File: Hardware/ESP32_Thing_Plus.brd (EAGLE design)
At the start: 33 x 58.9 mm, 54 parts, among them Q1 2.5A/30V, Q2 MBT3904DW1T1, U1 MCP73831, U2 ESP-WROOM-32, U3 AP2112K-3.3V, U4 FT231XS

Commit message: Feedback from review
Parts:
- removed C11, C14, C16, C3: 0.1uF, SparkFun-Capacitors:0603
- removed C12, C13: 47pF, SparkFun-Capacitors:0603
- removed C15: 4.7uF, SparkFun-Capacitors:0603-CAP
- removed C2: 10uF, SparkFun-Capacitors:0805
- removed D4: BLUE, SparkFun-LED:LED-0603
- removed F1: 6V/0.75A, SparkFun-Fuses:1206
- removed JP15: (no value), SparkFun-Connectors:USB-B-MICRO-SMD_V03
- removed R10: 10k, SparkFun-Resistors:0603
- removed R13, R14: 27, SparkFun-Resistors:0603
- removed S2: BTN-0, SparkFun-Electromechanical:TACTILE_SWITCH_SMD_4.6X2.8MM
- removed SJ1, SJ2: JUMPER-PAD-2-NC_BY_TRACE, SparkFun-Passives:PAD-JUMPER-2-NC_BY_TRACE_YES_SILK
- added J4: (no value), SparkFun-Connectors:1X16_NO_SILK
- added LOGO4: FOUR_LAYER_WARNING, SparkFun-Aesthetics:FOUR_LAYER_WARNING
- added R1: 1k, SparkFun-Resistors:0603
- added U$1: (no value), buzzard_labels:3V322
- added U$10: (no value), buzzard_labels:1611
- added U$11: (no value), buzzard_labels:1710
- added U$12: (no value), buzzard_labels:A020
- added U$13: (no value), buzzard_labels:A119
- added U$14: (no value), buzzard_labels:A218
- added U$15: (no value), buzzard_labels:A317
- added U$16: (no value), buzzard_labels:A416
- added U$17: (no value), buzzard_labels:A515
- added U$18: (no value), buzzard_labels:GND21
- added U$19: (no value), buzzard_labels:MISO12
- added U$2: (no value), buzzard_labels:138
- added U$20: (no value), buzzard_labels:MOSI13
- added U$21: (no value), buzzard_labels:SCK14
- added U$22: (no value), buzzard_labels:RESET23
- added U$23: (no value), buzzard_labels:SCL1
- added U$24: (no value), buzzard_labels:SDA0
- added U$25: (no value), buzzard_labels (1):CHG3
- added U$26: (no value), buzzard_labels (1):EN1
- added U$27, U$30: (no value), buzzard_labels (1):ESP32_THING_PLUS4
- added U$28: (no value), buzzard_labels (1):VBAT2
- added U$29: (no value), buzzard_labels (1):VUSB0
- added U$3: (no value), buzzard_labels:142
- added U$31: (no value), buzzard_labels (2):3V313
- added U$32: (no value), buzzard_labels (2):#RESET17
- added U$33: (no value), buzzard_labels (2):162
- added U$34: (no value), buzzard_labels (2):171
- added U$35: (no value), buzzard_labels (2):230
- added U$36: (no value), buzzard_labels (2):1326
- added U$37: (no value), buzzard_labels (2):1420
- added U$38: (no value), buzzard_labels (2):1522
- added U$39: (no value), buzzard_labels (2):2025
- added U$4: (no value), buzzard_labels:154
- added U$40: (no value), buzzard_labels (2):2724
- added U$41: (no value), buzzard_labels (2):3221
- added U$42: (no value), buzzard_labels (2):3323
- added U$43: (no value), buzzard_labels (2):A011
- added U$44: (no value), buzzard_labels (2):A29
- added U$45: (no value), buzzard_labels (2):A38
- added U$46: (no value), buzzard_labels (2):A47
- added U$47: (no value), buzzard_labels (2):A56
- added U$48: (no value), buzzard_labels (2):A110
- added U$49: (no value), buzzard_labels (2):EN16
- added U$5: (no value), buzzard_labels:207
- added U$50: (no value), buzzard_labels (2):GND12
- added U$51: (no value), buzzard_labels (2):MISO3
- added U$52: (no value), buzzard_labels (2):MOSI4
- added U$53: (no value), buzzard_labels (2):SCK5
- added U$54: (no value), buzzard_labels (2):SCL19
- added U$55: (no value), buzzard_labels (2):SDA18
- added U$56: (no value), buzzard_labels (2):VBAT15
- added U$57: (no value), buzzard_labels (2):VUSB14
- added U$58: (no value), buzzard_labels (3):QWIIC0
- added U$59: (no value), SparkFun-Aesthetics:ORDERING_INSTRUCTIONS
- added U$6: (no value), buzzard_labels:239
- added U$60: (no value), buzzard_labels (5):RESET0
- added U$7: (no value), buzzard_labels:276
- added U$8: (no value), buzzard_labels:323
- added U$9: (no value), buzzard_labels:335
- C1: value 0.1uF -> 10uF
- C10: value 2.2uF -> 1.0uF; device SparkFun-Capacitors:0603 -> SparkFun-Capacitors:0402
- D3: value RED -> BLUE
- FD1, FD2, FD3, FD4: device SparkFun-Aesthetics:MICRO-FIDUCIAL -> SparkFun-Aesthetics:FIDUCIAL-MICRO
- J1: value (none) -> AMP FCI 10103594-0001LF; device SparkFun-Connectors:1X20_NOSILK -> SparkFun-Connectors:USB-MICROB-PTH
- J2: device SparkFun-Connectors:1X20_NOSILK -> SparkFun-Connectors:1X12_NO_SILK
- JP2: device SparkFun-Connectors:JST-2-PTH -> SparkFun-Connectors:JST-2-SMD
- LOGO1: value SFE_LOGO_NAME.1_INCH -> SFE_LOGO_FLAME.1_INCH; device SparkFun-Aesthetics:SFE_LOGO_NAME_.1 -> SparkFun-Aesthetics:SFE_LOGO_FLAME_.1
- LOGO3: value SFE_LOGO_NAME.2_INCH -> SFE_LOGO_NAME_FLAME.1_INCH; device SparkFun-Aesthetics:SFE_LOGO_NAME_.2 -> SparkFun-Aesthetics:SFE_LOGO_NAME_FLAME_.1
- R4: value 1K -> 1k
- R5: value DNP -> 100K; device SparkFun-Passives:1/6W-RES -> SparkFun-Resistors:0402
- R8: value 330 -> 100K; device SparkFun-Resistors:0603 -> SparkFun-Resistors:0402
- R9: value 10k -> 100K; device SparkFun-Resistors:0603 -> SparkFun-Resistors:0402
- S1: device SparkFun-Electromechanical:TACTILE_SWITCH_SMD_4.6X2.8MM -> SparkFun-Switches:TACTILE_SWITCH_SMD_4.6X2.8MM
- U2: value ESP-WROOM-32 -> ESP-WROOM-32NARROW; device SparkFun-RF:ESP-WROOM-32 -> SparkFun-RF:ESP-WROOM-32-NARROW
- U4: value FT231XS -> CP2102N; device SparkFun-DigitalIC:SSOP20_L -> SparkFun-IC-Comms:QFN24
- moved FD4 60.3 mm to (1.27, 5.08)
- moved FD1 45.1 mm to (21.6, 48.3)
- moved R2 39.8 mm to (18.3, 10.7)
- moved J2 34.1 mm to (1.27, 16.5)
- moved C1 30.3 mm to (9.53, 22.1), turned to 0 degrees
- moved LOGO2 29.5 mm to (5.71, 2.92)
- moved R9 24.6 mm to (5.08, 5.84), turned to 0 degrees
- moved R8 22.9 mm to (9.27, 14.5), turned to 0 degrees
- moved J3 22.0 mm to (4.83, 10.8), flipped to the bottom, turned to 90 degrees
- moved D3 21.1 mm to (6.10, 22.0), turned to 0 degrees
- moved LOGO1 20.8 mm to (9.02, 5.84), turned to 0 degrees
- moved R4 18.7 mm to (6.10, 23.2), turned to 180 degrees
- moved C6 17.7 mm to (3.94, 17.7), turned to 90 degrees
- moved S1 17.2 mm to (17.7, 7.11), turned to 180 degrees
- moved JP2 16.5 mm to (3.30, 10.8), turned to 90 degrees
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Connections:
- net N$9 renamed CHG
- removed net 18: J2.12, U2.30
- removed net 19: J2.13, U2.31
- removed net 21: J2.15, J3.3, U2.33
- removed net 22: J2.18, J3.4, U2.36
- removed net 25: J1.16, U2.10
- removed net 26: J1.15, U2.11
- removed net 3.3V_F: C16.1, U4.13, U4.14, U4.3
- removed net 34: J1.20, U2.6
- removed net 4: J2.8, U2.26
- removed net 5: D4.A, J2.11, U2.29
- removed net N$16: R6.2, SJ1.1
- removed net N$3: R4.1, SJ2.1
- removed net N$7: R13.2, U4.12
- removed net N$8: R14.2, U4.11
- removed net SHIELD: JP15.SHIELD1, JP15.SHIELD2, JP15.SHIELD3
- removed net U0RXD: J2.16, U2.34, U4.20
- removed net U0TXD: J2.17, U2.35, U4.4
- removed net VUSB-RAW: C11.1, F1.1, J1.2, J2.2, JP15.VBUS
- new net A0: J4.5, U2.11
- new net A1: J4.6, U2.10
- new net A2: J4.7, U2.6
- new net A3: J4.8, U2.5
- new net A4: J4.9, U2.4
- new net A5: J4.10, U2.26
- new net EN: J2.2, R8.2, U3.3
- new net MISO: J4.13, U2.31
- new net MOSI: J4.12, U2.30
- new net RX: U2.35, U4.20
- new net SCK: J4.11, U2.29
- new net SCL: J2.11, J3.4, U2.36
- new net SDA: J2.12, J3.3, U2.33
- new net TX: U2.34, U4.21
- new net VDD: U4.6
- net 0: no longer J2.7, R9.1, S2.3, S2.4
- net 12: no longer J1.12, R10.2
- net 13: now also J2.4, R4.1; no longer J1.11
- net 14: now also J2.10; no longer J1.13
- net 15: now also J2.8; no longer J1.10
- net 16: now also J4.14; no longer J2.9
- net 17: now also J4.15; no longer J2.10
- net 2: no longer J2.6
- net 20: now also J2.5; no longer J2.14
- net 23: now also J4.16; no longer J2.19
- net 27: now also J2.6; no longer J1.14
- net 3.3V: now also J4.2, R1.1, U4.5; no longer C2.1, J1.5, J2.5, R9.2, SJ2.2
- net 32: now also J2.9; no longer J1.18
- net 33: now also J2.7; no longer J1.17
- net 35: now also R5.1, R9.2; no longer J1.19
- net CHIP_PU: now also J4.1; no longer C3.1, J1.6, S1.3
- net D+: now also J1.D+, U4.3; no longer C13.1, JP15.D+, R14.1
- net D-: now also J1.D-, U4.4; no longer C12.1, JP15.D-, R13.1
- net DTR: now also U4.23; no longer U4.1
- net GND: now also J1.GND, J4.4, JP2.2, R9.1, U4.2, U4.PAD; no longer C11.2, C12.2, C13.2, C14.2, C15.2, C16.2, C2.2, C3.2, J1.1, J1.4, J1.7, J1.8, J1.9, J2.1, J2.20, J2.4, JP15.GND, JP2.1, R10.1, R5.1, R8.1, S1.2, S2.1, S2.2, U4.16, U4.6
- net N$1: now also R1.2, U4.9; no longer D4.C, R8.2
- net N$14: now also R6.2; no longer R5.2, SJ1.2
- net RTS: now also U4.19; no longer U4.2
- net VIN: now also R8.1; no longer U3.3
- net V_BATT: now also J2.1, JP2.1, R5.2; no longer J1.3, J2.3, JP2.2
- net V_USB: now also J1.VBUS, J2.3, U4.7; no longer C14.1, C15.1, F1.2, U4.15
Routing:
- net 3.3V: track 111.3 -> 26.5 mm, vias 5 -> 6
- net 21: track 66.8 -> 0.00 mm, vias 2 -> 0
- net 22: track 65.2 -> 0.00 mm, vias 2 -> 0
- net SDA: track 0.00 -> 62.1 mm
- net U0RXD: track 61.2 -> 0.00 mm, vias 2 -> 0
- net U0TXD: track 53.3 -> 0.00 mm, vias 2 -> 0
- net SCL: track 0.00 -> 51.1 mm, vias 0 -> 1
- net 0: track 52.6 -> 7.26 mm, vias 3 -> 0
- net VUSB-RAW: track 40.6 -> 0.00 mm, vias 1 -> 0
- net V_USB: track 43.2 -> 9.94 mm, vias 4 -> 6
- net A2: track 0.00 -> 30.7 mm, vias 0 -> 1
- net A3: track 0.00 -> 30.4 mm, vias 0 -> 1
- net V_BATT: track 56.3 -> 26.3 mm, vias 3 -> 0
- net A4: track 0.00 -> 29.8 mm, vias 0 -> 1
- net TX: track 0.00 -> 29.2 mm, vias 0 -> 2
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- added copper zone on layer 15, net 3.3V
- added copper zone on layer 2, net GND
- added copper zone on layer 15, net V_USB
- removed copper zone on layer 1, net GND
- removed copper zone on layer 16, net GND
- removed copper zone on layer 1, net SHIELD
- removed copper zone on layer 16, net SHIELD
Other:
- board size 33 x 58.9 mm -> 22.9 x 50.8 mm
- board text added: "+"
- board text added: "-"
- board text added: "1"
- board text added: "3"
- board text removed: "!RST"
- board text removed: "0"
- board text removed: "12"
- board text removed: "13"
- board text removed: "14"
- board text removed: "15"
- board text removed: "16"
- board text removed: "17"
- board text removed: "18"
- board text removed: "19"
- board text removed: "20"
- board text removed: "21"
- board text removed: "22"
- board text removed: "23"
- board text removed: "25"
- board text removed: "26"
- board text removed: "27"
- board text removed: "32"
- board text removed: "33"
- board text removed: "34"
- board text removed: "35"
- board text removed: "3V3"
- board text removed: "5"
- board text removed: "C"
- board text removed: "CHG PROG"
- board text removed: "ESP32 Thing Plus"
- board text removed: "GND"
- board text removed: "LED5"
- board text removed: "Measurements in inches"
- board text removed: "P"
- board text removed: "PWR LED"
- board text removed: "QWIIC"
- board text removed: "RST"
- board text removed: "RX"
- board text removed: "RXI"
- board text removed: "TX"
- board text removed: "TXO"
- board text removed: "VBAT"
- board text removed: "VUSB"

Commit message: Fixes after QC review
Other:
- board text added: "Units in inches"
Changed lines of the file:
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@@
 <layers>
 <layer number="1" name="Top" color="4" fill="1" visible="yes" active="yes"/>
-<layer number="2" name="Route2" color="1" fill="3" visible="yes" active="yes"/>
-<layer number="15" name="Route15" color="4" fill="6" visible="yes" active="yes"/>
+<layer number="2" name="Route2" color="1" fill="3" visible="no" active="yes"/>
+<layer number="15" name="Route15" color="4" fill="6" visible="no" active="yes"/>
 <layer number="16" name="Bottom" color="1" fill="1" visible="yes" active="yes"/>
 <layer number="17" name="Pads" color="2" fill="1" visible="yes" active="yes"/>
@@
 <layer number="29" name="tStop" color="7" fill="3" visible="no" active="yes"/>
 <layer number="30" name="bStop" color="7" fill="6" visible="no" active="yes"/>
-<layer number="31" name="tCream" color="7" fill="4" visible="yes" active="yes"/>
+<layer number="31" name="tCream" color="7" fill="4" visible="no" active="yes"/>
 <layer number="32" name="bCream" color="7" fill="5" visible="no" active="yes"/>
-<layer number="39" name="tKeepout" color="4" fill="11" visible="yes" active="yes"/>
+<layer number="39" name="tKeepout" color="4" fill="11" visible="no" active="yes"/>
 <layer number="40" name="bKeepout" color="1" fill="11" visible="no" active="yes"/>
 <layer number="41" name="tRestrict" color="4" fill="10" visible="no" active="yes"/>
@@
 <text x="8.636" y="8.255" size="0.8128" layer="21" font="vector" ratio="15">+</text>
 <text x="8.636" y="12.319" size="0.8128" layer="21" font="vector" ratio="15">-</text>
+<text x="27.94" y="-2.54" size="1.27" layer="47" font="vector" ratio="15">Units in inches</text>
 </plain>
 <attributes>

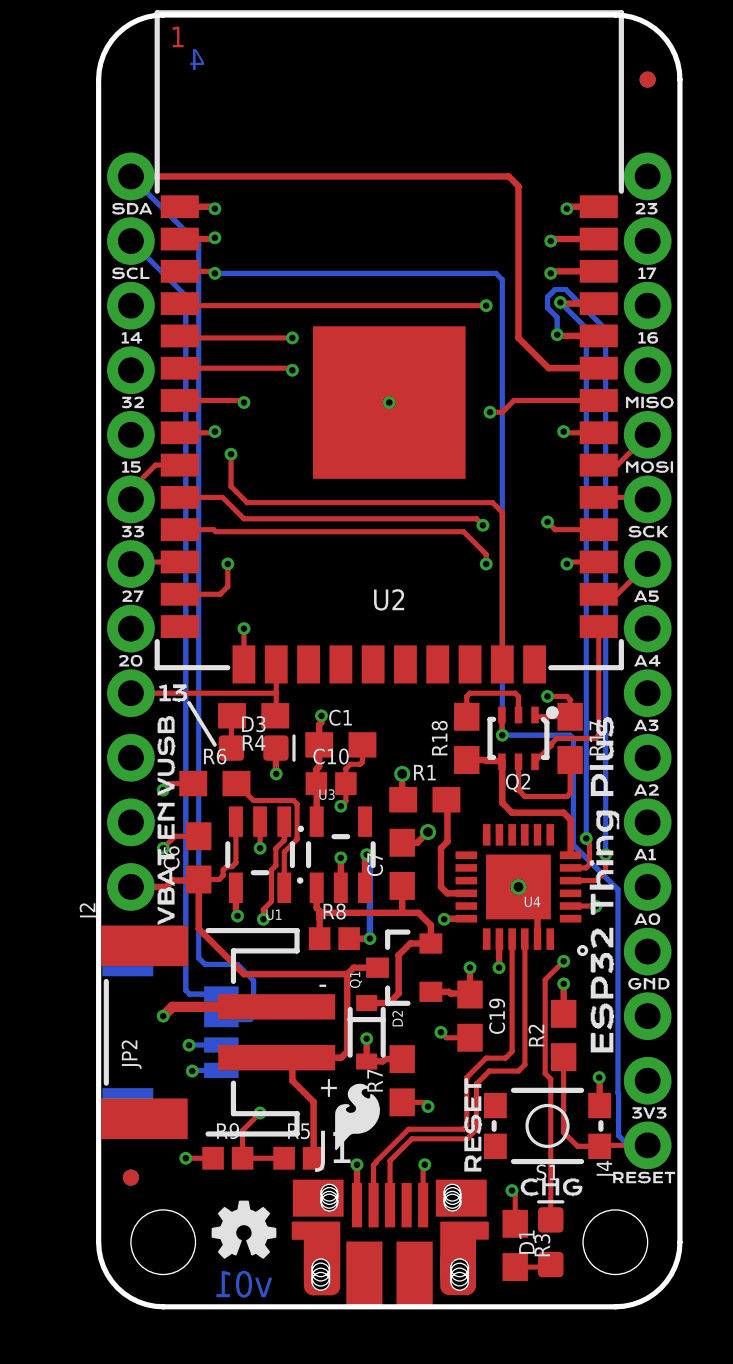
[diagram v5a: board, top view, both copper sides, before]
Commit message: Changes from review, changed silk
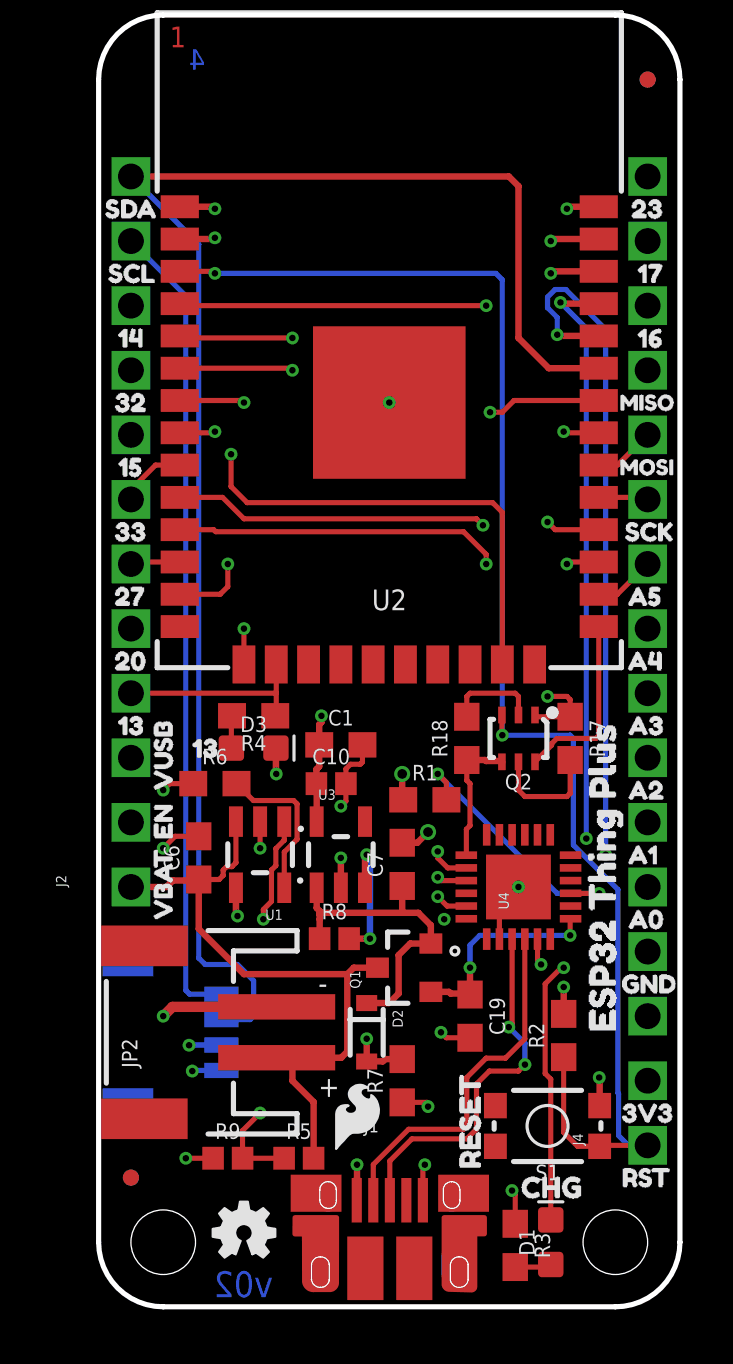
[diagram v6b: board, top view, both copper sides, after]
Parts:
- added U$61: (no value), buzzard_labels (43):ESP32_THING_PLUS0
- J1: device SparkFun-Connectors:USB-MICROB-PTH -> SparkFun-Connectors:USB-MICROB-PTH-MILL
- J2: device SparkFun-Connectors:1X12_NO_SILK -> SparkFun-Connectors:1X12_SM_SQ_NOSILK
- J4: device SparkFun-Connectors:1X16_NO_SILK -> SparkFun-Connectors:1X16_SM_SQ_NOSILK
- U$1: device buzzard_labels:3V322 -> buzzard_labels (37):#RESET0
- U$10: device buzzard_labels:1611 -> buzzard_labels (37):2721
- U$11: device buzzard_labels:1710 -> buzzard_labels (37):3218
- U$12: device buzzard_labels:A020 -> buzzard_labels (37):3320
- U$13: device buzzard_labels:A119 -> buzzard_labels (37):A03
- U$14: device buzzard_labels:A218 -> buzzard_labels (37):A14
- U$15: device buzzard_labels:A317 -> buzzard_labels (37):A25
- U$16: device buzzard_labels:A416 -> buzzard_labels (37):A36
- U$17: device buzzard_labels:A515 -> buzzard_labels (37):A47
- U$18: device buzzard_labels:GND21 -> buzzard_labels (37):A58
- U$19: device buzzard_labels:MISO12 -> buzzard_labels (37):EN26
- U$2: device buzzard_labels:138 -> buzzard_labels (37):3V31
- U$20: device buzzard_labels:MOSI13 -> buzzard_labels (37):GND2
- U$21: device buzzard_labels:SCK14 -> buzzard_labels (37):MISO11
- U$22: device buzzard_labels:RESET23 -> buzzard_labels (37):MOSI10
- U$23: device buzzard_labels:SCL1 -> buzzard_labels (37):QWIIC27
- U$24: device buzzard_labels:SDA0 -> buzzard_labels (37):SCK9
- U$25: device buzzard_labels (1):CHG3 -> buzzard_labels (37):SCL16
- U$26: device buzzard_labels (1):EN1 -> buzzard_labels (37):SDA15
- U$27: device buzzard_labels (1):ESP32_THING_PLUS4 -> buzzard_labels (37):VBAT25
- U$28: device buzzard_labels (1):VBAT2 -> buzzard_labels (37):VUSB24
- U$29: device buzzard_labels (1):VUSB0 -> buzzard_labels (38):SDA0
- U$3: device buzzard_labels:142 -> buzzard_labels (37):1323
- U$30: device buzzard_labels (1):ESP32_THING_PLUS4 -> buzzard_labels (39):3V312
- U$31: device buzzard_labels (2):3V313 -> buzzard_labels (39):137
- U$32: device buzzard_labels (2):#RESET17 -> buzzard_labels (39):141
- U$33: device buzzard_labels (2):162 -> buzzard_labels (39):153
- U$34: device buzzard_labels (2):171 -> buzzard_labels (39):206
- U$35: device buzzard_labels (2):230 -> buzzard_labels (39):275
- U$36: device buzzard_labels (2):1326 -> buzzard_labels (39):322
- U$37: device buzzard_labels (2):1420 -> buzzard_labels (39):334
- U$38: device buzzard_labels (2):1522 -> buzzard_labels (39):1623
- U$39: device buzzard_labels (2):2025 -> buzzard_labels (39):1724
- U$4: device buzzard_labels:154 -> buzzard_labels (37):1417
- U$40: device buzzard_labels (2):2724 -> buzzard_labels (39):2325
- U$41: device buzzard_labels (2):3221 -> buzzard_labels (39):A014
- U$42: device buzzard_labels (2):3323 -> buzzard_labels (39):A115
- U$43: device buzzard_labels (2):A011 -> buzzard_labels (39):A216
- U$44: device buzzard_labels (2):A29 -> buzzard_labels (39):A317
- U$45: device buzzard_labels (2):A38 -> buzzard_labels (39):A418
- U$46: device buzzard_labels (2):A47 -> buzzard_labels (39):A519
- U$47: device buzzard_labels (2):A56 -> buzzard_labels (39):SCK20
- U$48: device buzzard_labels (2):A110 -> buzzard_labels (39):RST11
- U$49: device buzzard_labels (2):EN16 -> buzzard_labels (39):GND13
- U$5: device buzzard_labels:207 -> buzzard_labels (37):1519
- U$50: device buzzard_labels (2):GND12 -> buzzard_labels (39):VUSB8
- U$51: device buzzard_labels (2):MISO3 -> buzzard_labels (39):EN9
- U$52: device buzzard_labels (2):MOSI4 -> buzzard_labels (39):VBAT10
- U$53: device buzzard_labels (2):SCK5 -> buzzard_labels (39):137
- U$54: device buzzard_labels (2):SCL19 -> buzzard_labels (40):MISO0
- U$55: device buzzard_labels (2):SDA18 -> buzzard_labels (40):MOSI1
- U$56: device buzzard_labels (2):VBAT15 -> buzzard_labels (41):CHG1
- U$57: device buzzard_labels (2):VUSB14 -> buzzard_labels (41):RESET0
- U$58: device buzzard_labels (3):QWIIC0 -> buzzard_labels (42):ESP32_THING_PLUS0
- U$6: device buzzard_labels:239 -> buzzard_labels (37):1612
- U$60: device buzzard_labels (5):RESET0 -> buzzard_labels (39):SCL0
- U$7: device buzzard_labels:276 -> buzzard_labels (37):1713
- U$8: device buzzard_labels:323 -> buzzard_labels (37):2022
- U$9: device buzzard_labels:335 -> buzzard_labels (37):2314
- moved U$30 41.8 mm to (19.9, 7.62), flipped to the top
- moved U$60 38.9 mm to (-0.25, 40.6), turned to 0 degrees
- moved U$25 38.5 mm to (6.10, 41.9), flipped to the bottom
- moved U$32 38.3 mm to (0.13, 38.1), flipped to the top
- moved U$22 29.2 mm to (21.2, 34.3), flipped to the bottom
- moved U$23 28.4 mm to (6.60, 13.0), flipped to the bottom, turned to 270 degrees
- moved U$52 27.1 mm to (2.54, 14.6), flipped to the top, turned to 90 degrees
- moved U$26 26.9 mm to (6.22, 44.5), flipped to the bottom, turned to 0 degrees
- moved U$35 26.9 mm to (0.00, 27.9), flipped to the top
- moved U$34 26.9 mm to (0.00, 25.4), flipped to the top
- moved U$51 26.7 mm to (2.54, 17.8), flipped to the top, turned to 90 degrees
- moved U$41 26.4 mm to (20.2, 15.2), flipped to the top
- moved U$31 25.3 mm to (0.13, 22.9), flipped to the top
- moved U$9 25.0 mm to (21.2, 44.5), flipped to the bottom
- moved U$7 25.0 mm to (21.2, 41.9), flipped to the bottom
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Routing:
- net N$1: track 4.65 -> 10.6 mm, vias 0 -> 2
- net TX: track 29.2 -> 35.2 mm, vias 2 -> 3
- net RX: track 24.9 -> 30.6 mm, vias 2 -> 3
- net V_USB: track 9.94 -> 15.6 mm, vias 6 -> 7
- net DTR: track 13.1 -> 17.6 mm
- net RTS: track 7.39 -> 5.29 mm
- net CHG: track 27.5 -> 29.5 mm
- net 3.3V: track 26.5 -> 24.6 mm
- net D+: track 14.6 -> 14.7 mm, vias 0 -> 2
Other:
- board text added: "v02"
- board text removed: "Original ESP32 Thing Design by Jim Lindblom"
- board text removed: "v01"
